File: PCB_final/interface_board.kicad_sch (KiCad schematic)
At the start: 116 parts, among them J1 02x30_Shift_Register_Connector, J2 02x30_ADC_Connector, J5 PicoPinSocketB, J6 PicoPinSocketA, U1 74HC595, U10 MCP6001T-I_OT, U2 74HC595, U3 74HC595, U4 74HC595, U5 74HC595, U6 74HC595, U7 74HC595, U8 MAX11643EEG, U9 MAX11643EEG

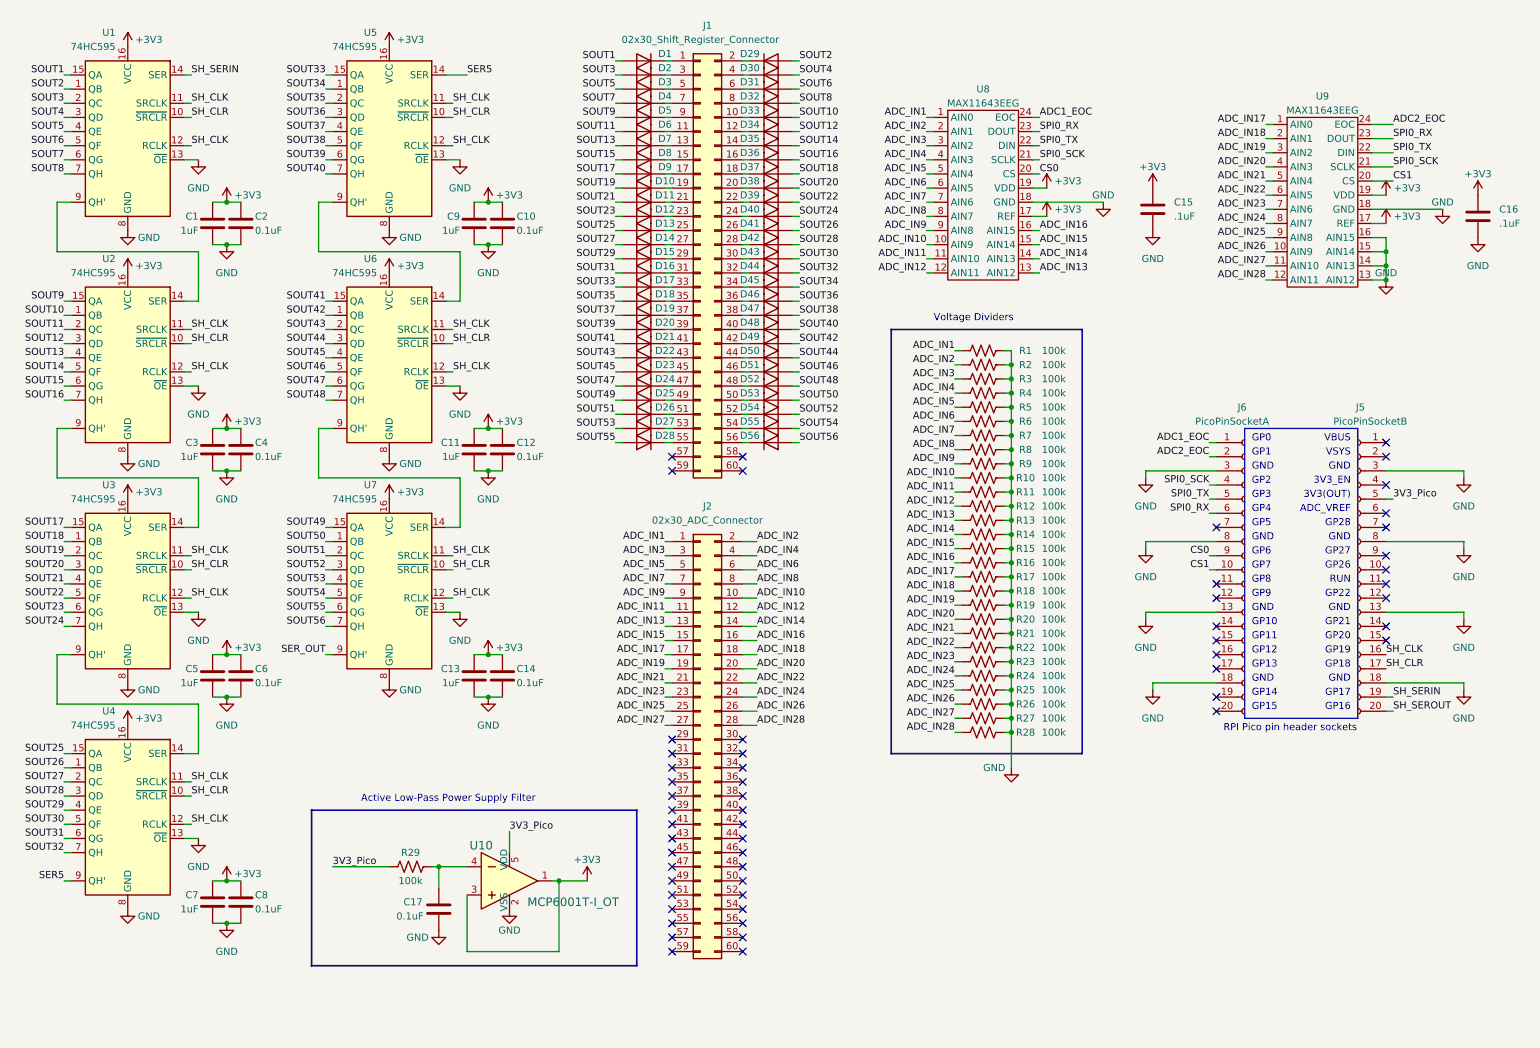
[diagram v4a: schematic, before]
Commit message: Found naming errors with schematic and a few traces in PCB that weren't connected correctly. PCB now passes DRC with only a few warnings about silkscreen
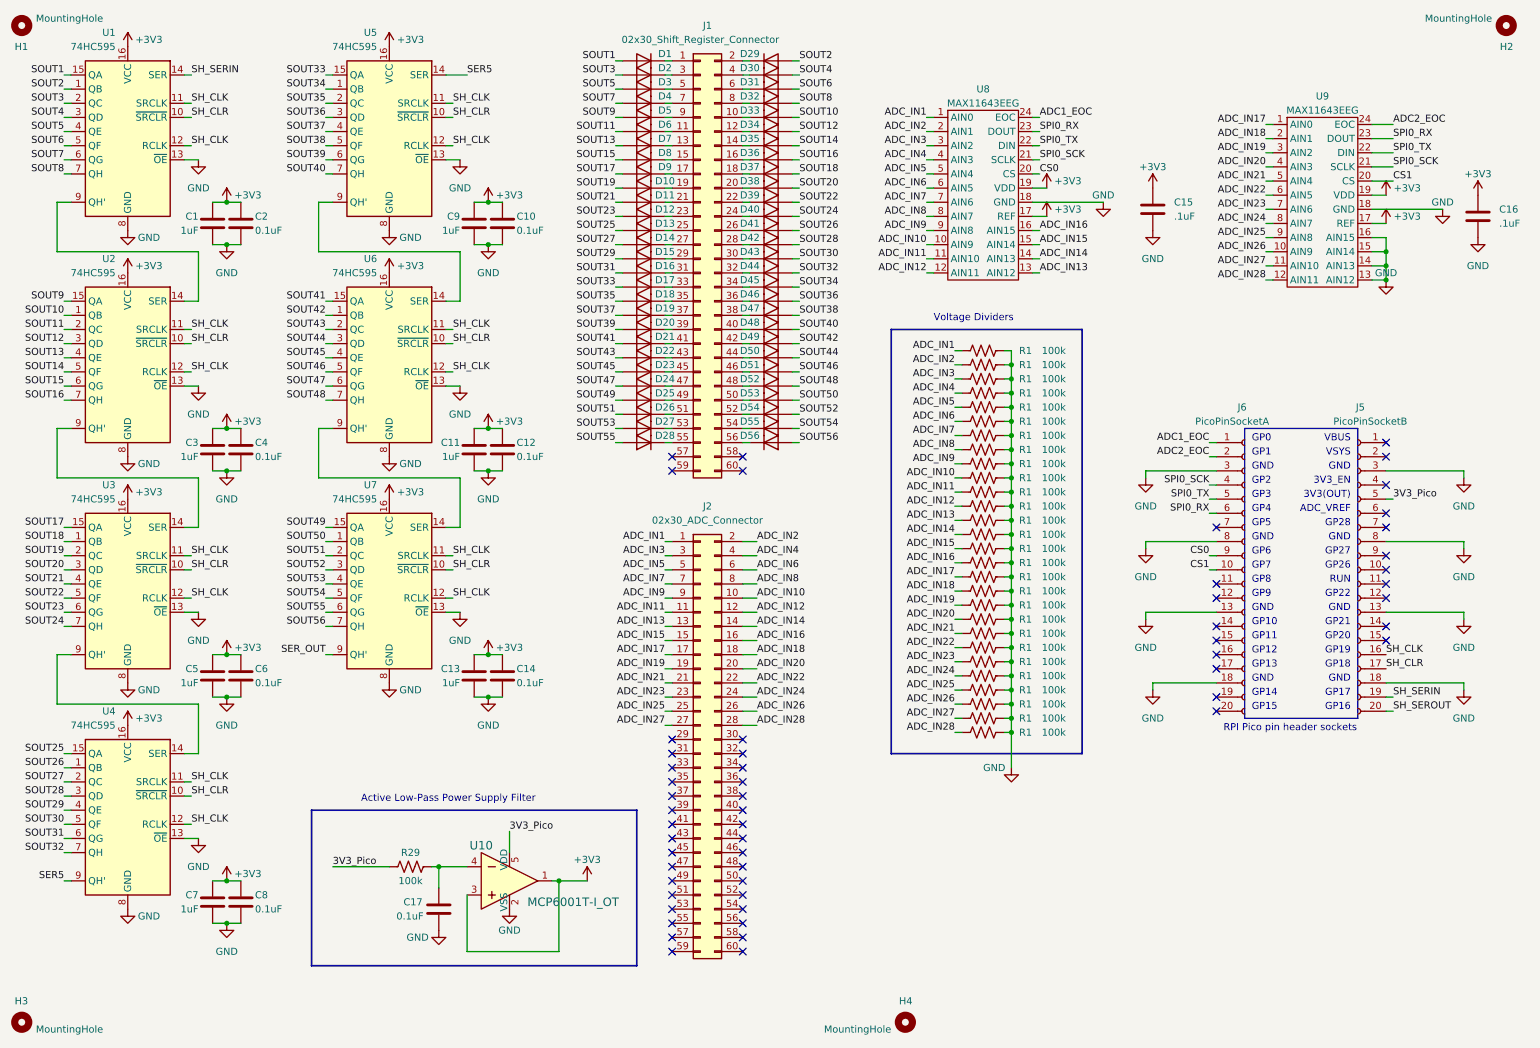
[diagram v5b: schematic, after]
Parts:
- removed R10, R11, R12, R13, R14, R15, R16, R17, R18, R19, R2, R20, R21, R22, R23, R24, R25, R26, R27, R28, R3, R4, R5, R6, R7, R8, R9: 100k, Resistor_SMD:R_0603_1608Metric, symbol Device:R_US
- added H1, H2, H3, H4: MountingHole, MountingHole:MountingHole_2.2mm_M2, symbol Mechanical:MountingHole
- added R1 (x27): 100k, Resistor_SMD:R_0603_1608Metric, symbol Device:R_US
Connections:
- net ADC_IN10: now also R1.1
- net ADC_IN11: now also R1.1
- net ADC_IN12: now also R1.1
- net ADC_IN13: now also R1.1
- net ADC_IN14: now also R1.1
- net ADC_IN15: now also R1.1
- net ADC_IN16: now also R1.1
- net ADC_IN17: now also R1.1
- net ADC_IN18: now also R1.1
- net ADC_IN19: now also R1.1
- net ADC_IN2: now also R1.1
- net ADC_IN20: now also R1.1
- net ADC_IN21: now also R1.1
- net ADC_IN22: now also R1.1
- net ADC_IN23: now also R1.1
- net ADC_IN24: now also R1.1
- net ADC_IN25: now also R1.1
- net ADC_IN26: now also R1.1
- net ADC_IN27: now also R1.1
- net ADC_IN28: now also R1.1
- net ADC_IN3: now also R1.1
- net ADC_IN4: now also R1.1
- net ADC_IN5: now also R1.1
- net ADC_IN6: now also R1.1
- net ADC_IN7: now also R1.1
- net ADC_IN8: now also R1.1
- net ADC_IN9: now also R1.1
- net GND: now also R1.2, R1.2, R1.2, R1.2, R1.2, R1.2, R1.2, R1.2, R1.2, R1.2, R1.2, R1.2, R1.2, R1.2, R1.2, R1.2, R1.2, R1.2, R1.2, R1.2, R1.2, R1.2, R1.2, R1.2, R1.2, R1.2, R1.2

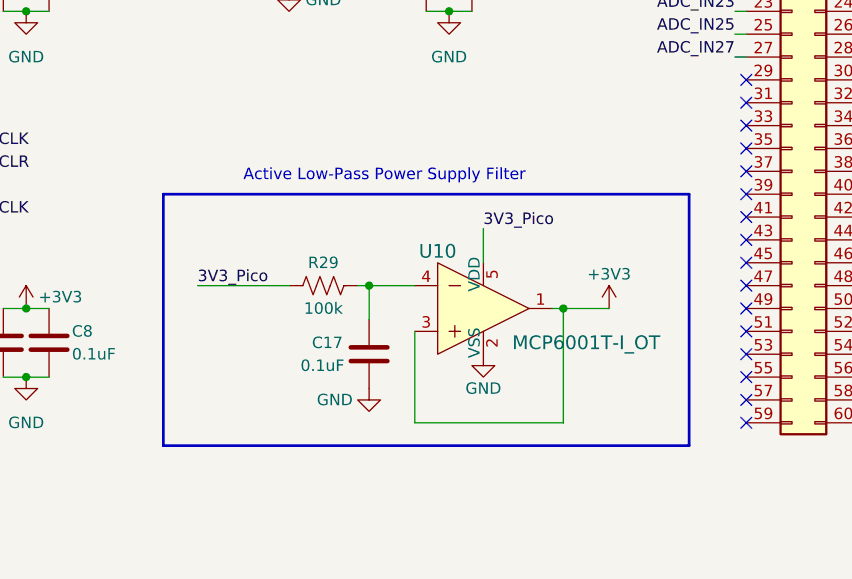
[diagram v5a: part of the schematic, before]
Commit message: Moved active low pass op-amp filter to its own schematic sheet
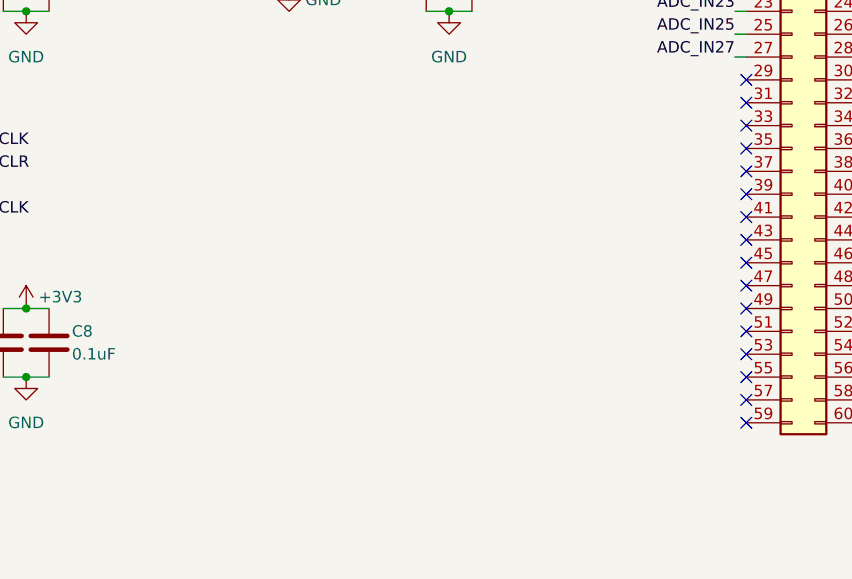
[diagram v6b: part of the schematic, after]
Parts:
- removed C17: 0.1uF, Capacitor_SMD:C_0603_1608Metric, symbol Device:C
- removed R29: 100k, Resistor_SMD:R_0603_1608Metric, symbol Device:R_US
- removed U10: MCP6001T-I_OT, digikey-footprints:SOT-753, symbol dk_Linear-Amplifiers-Instrumentation-OP-Amps-Buffer-Amps:MCP6001T-I_OT
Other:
- note removed: "Active Low-Pass Power Supply Filter"

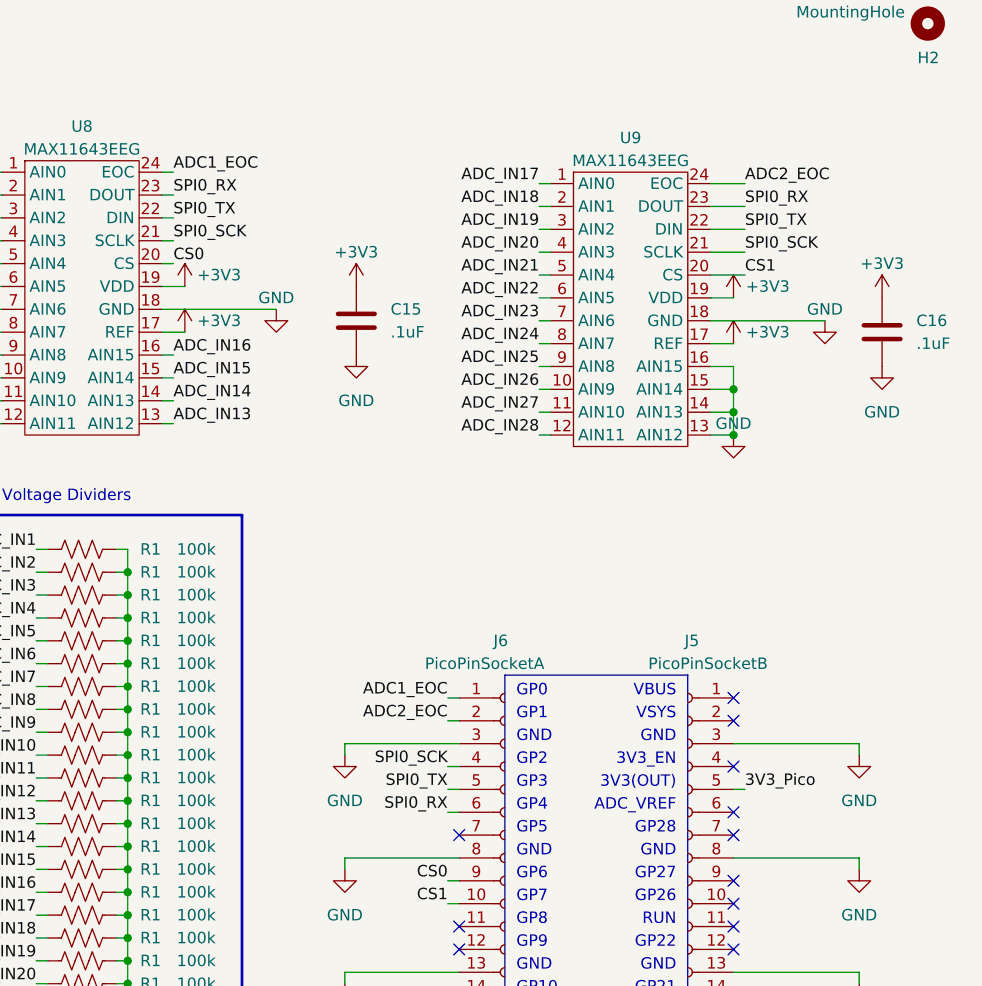
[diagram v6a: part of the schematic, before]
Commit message: Removed filter from schematic and PCB. Adjusted tracings on PCB and schematic for ADC inputs so that each ADC has 14 inputs
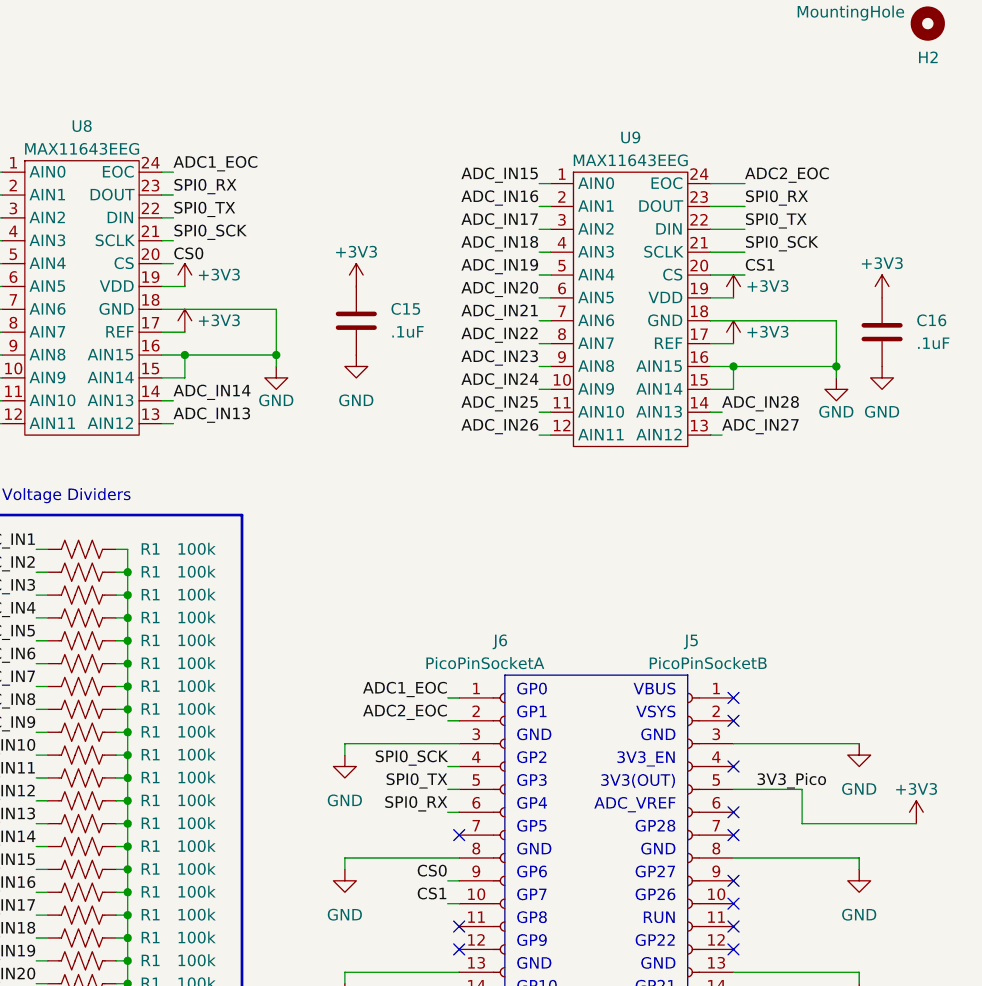
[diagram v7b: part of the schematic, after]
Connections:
- net 3V3_Pico is gone; now on net +3V3: J5.5 (Pin_5)
- net ADC_IN15: now also U9.1 (AIN0); no longer U8.15 (AIN14)
- net ADC_IN16: now also U9.2 (AIN1); no longer U8.16 (AIN15)
- net ADC_IN17: now also U9.3 (AIN2); no longer U9.1 (AIN0)
- net ADC_IN18: now also U9.4 (AIN3); no longer U9.2 (AIN1)
- net ADC_IN19: now also U9.5 (AIN4); no longer U9.3 (AIN2)
- net ADC_IN20: now also U9.6 (AIN5); no longer U9.4 (AIN3)
- net ADC_IN21: now also U9.7 (AIN6); no longer U9.5 (AIN4)
- net ADC_IN22: now also U9.8 (AIN7); no longer U9.6 (AIN5)
- net ADC_IN23: now also U9.9 (AIN8); no longer U9.7 (AIN6)
- net ADC_IN24: now also U9.10 (AIN9); no longer U9.8 (AIN7)
- net ADC_IN25: now also U9.11 (AIN10); no longer U9.9 (AIN8)
- net ADC_IN26: now also U9.12 (AIN11); no longer U9.10 (AIN9)
- net ADC_IN27: now also U9.13 (AIN12); no longer U9.11 (AIN10)
- net ADC_IN28: now also U9.14 (AIN13); no longer U9.12 (AIN11)
- net GND: now also U8.15 (AIN14), U8.16 (AIN15); no longer U9.13 (AIN12), U9.14 (AIN13)

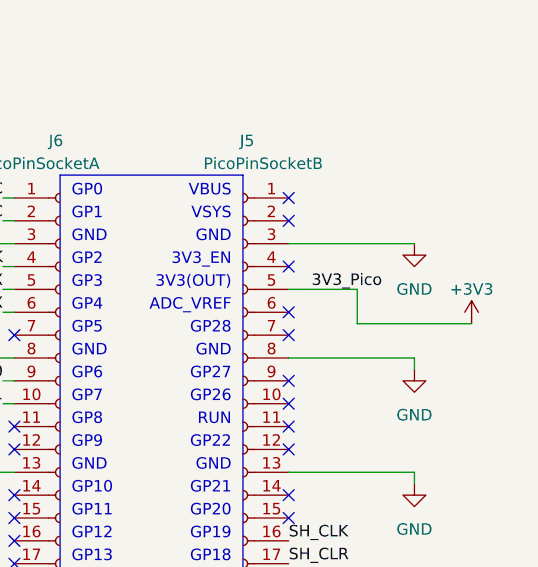
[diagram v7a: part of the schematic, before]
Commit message: Updated filter's ferrite bead and capacitors on schematic and PCB. Power supply filter now fully integrated
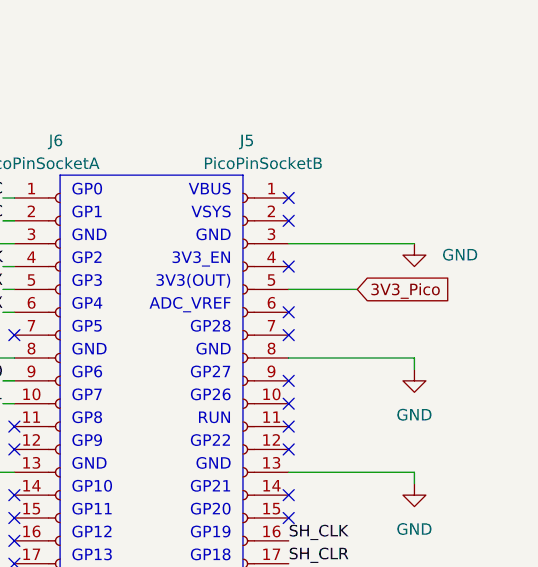
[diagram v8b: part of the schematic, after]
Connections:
- net +3V3: no longer J5.5 (Pin_5)
- new net 3V3_Pico: J5.5 (Pin_5)
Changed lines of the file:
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@@
     (stroke (width 0) (type default))
   )
-  (wire (pts (xy 267.97 100.33) (xy 267.97 104.14))
-    (stroke (width 0) (type default))
-  )
   (wire (pts (xy 22.86 72.39) (xy 24.13 72.39))
     (stroke (width 0) (type default))
@@
     (stroke (width 0) (type default))
   )
-  (wire (pts (xy 267.97 104.14) (xy 280.67 104.14))
-    (stroke (width 0) (type default))
-  )
   (wire (pts (xy 274.32 109.22) (xy 274.32 107.95))
     (stroke (width 0) (type default))
@@
     (effects (font (size 1.27 1.27)) (justify left bottom))
   )
-  (label "3V3_Pico" (at 262.89 100.33 0) (fields_autoplaced)
-    (effects (font (size 1.27 1.27)) (justify left bottom))
-  )
   (label "SOUT7" (at 22.86 39.37 180) (fields_autoplaced)
     (effects (font (size 1.27 1.27)) (justify right bottom))
@@
     (effects (font (size 1.27 1.27)) (justify left bottom))
   )
+  (global_label "3V3_Pico" (shape input) (at 267.97 100.33 0) (fields_autoplaced)
+    (effects (font (size 1.27 1.27)) (justify left))
+    (property "Intersheetrefs" "${INTERSHEET_REFS}" (at 279.5428 100.33 0)
+      (effects (font (size 1.27 1.27)) (justify left) hide)
+    )
+  )
   (symbol (lib_id "power:+3V3") (at 34.29 140.97 0) (unit 1)
     (in_bom yes) (on_board yes) (dnp no)
@@
     )
   )
-  (symbol (lib_id "power:+3V3") (at 280.67 104.14 0) (unit 1)
-    (in_bom yes) (on_board yes) (dnp no)
-    (property "Reference" "#PWR09" (at 280.67 107.95 0)
-      (effects (font (size 1.27 1.27)) hide)
-    )
-    (property "Value" "+3V3" (at 280.67 100.33 0)
-      (effects (font (size 1.27 1.27)))
-    )
-    (property "Footprint" "" (at 280.67 104.14 0)
-      (effects (font (size 1.27 1.27)) hide)
-    )
-    (property "Datasheet" "" (at 280.67 104.14 0)
-      (effects (font (size 1.27 1.27)) hide)
-    )
-    (pin "1")
-    (instances
-      (project "interface_board"
-        (path "/2096cfcb-1c5f-4ebc-ae85-e59f8ec52ec3"
-          (reference "#PWR09") (unit 1)
-        )
-      )
-      (project "PCB_final"
-        (path "/e4192969-4b4c-4bbf-a0a8-ef09d84e64d7"
-          (reference "#PWR09") (unit 1)
-        )
-        (path "/e4192969-4b4c-4bbf-a0a8-ef09d84e64d7/e0559890-1aa0-4336-9a3e-110d23fe279d"
-          (reference "#PWR051") (unit 1)
-        )
-      )
-    )
-  )
   (symbol (lib_id "Diode:MMSD4148") (at 149.86 80.01 0) (mirror x) (unit 1)
     (in_bom yes) (on_board yes) (dnp no)
@@
   )
   (symbol (lib_id "power:GND") (at 274.32 95.25 0) (unit 1)
-    (in_bom yes) (on_board yes) (dnp no) (fields_autoplaced)
+    (in_bom yes) (on_board yes) (dnp no)
     (property "Reference" "#PWR023" (at 274.32 101.6 0)
       (effects (font (size 1.27 1.27)) hide)
     )
-    (property "Value" "GND" (at 274.32 100.33 0)
+    (property "Value" "GND" (at 279.4 96.52 0)
       (effects (font (size 1.27 1.27)))
     )
